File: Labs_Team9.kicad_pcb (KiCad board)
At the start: 2 copper layers, 34.8 x 24.7 mm, 14 parts, among them J1 Conn_02x04_Counter_Clockwise, SW1 SW_Push, SW2 SW_Push, U1 STM32F411RETx, Y1 Crystal_GND24

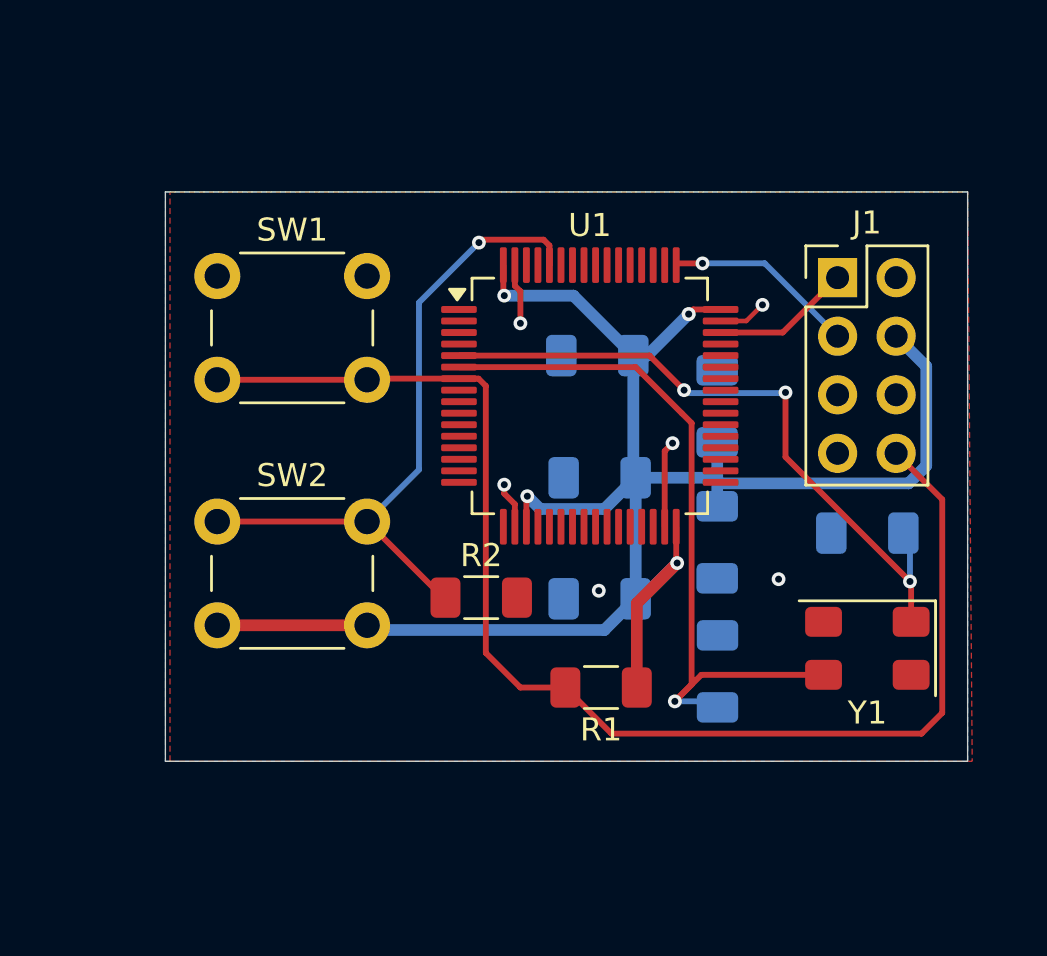
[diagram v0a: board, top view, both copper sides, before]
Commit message: lab2: add schematic and part of the trace
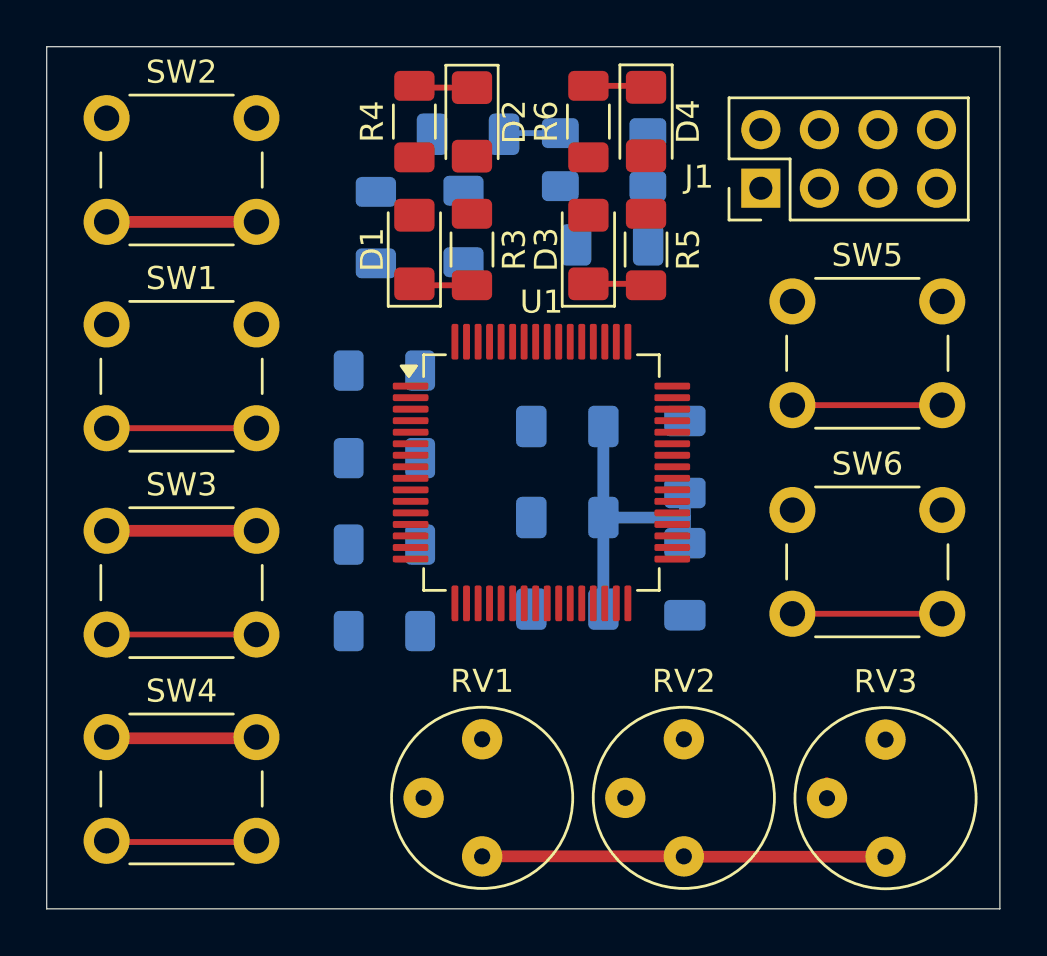
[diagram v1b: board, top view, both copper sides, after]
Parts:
- added D1: LED, LED_SMD:LED_1206_3216Metric_Pad1.42x1.75mm_HandSolder, F.Cu at (148.1, 91.2)
- added D2: LED, LED_SMD:LED_1206_3216Metric_Pad1.42x1.75mm_HandSolder, F.Cu at (150.6, 85.7)
- added D3: LED, LED_SMD:LED_1206_3216Metric_Pad1.42x1.75mm_HandSolder, F.Cu at (155.7, 91.2)
- added D4: LED, LED_SMD:LED_1206_3216Metric_Pad1.42x1.75mm_HandSolder, F.Cu at (158.2, 85.7)
- added R10: 10 kOhm, Resistor_SMD:R_1206_3216Metric_Pad1.30x1.75mm_HandSolder, B.Cu at (150.2, 90.2)
- added R3: 510 Ohm, Resistor_SMD:R_1206_3216Metric_Pad1.30x1.75mm_HandSolder, F.Cu at (150.6, 91.2)
- added R4: 680 Ohm, Resistor_SMD:R_1206_3216Metric_Pad1.30x1.75mm_HandSolder, F.Cu at (148.1, 85.7)
- added R5: 680 Ohm, Resistor_SMD:R_1206_3216Metric_Pad1.30x1.75mm_HandSolder, F.Cu at (158.2, 91.2)
- added R6: 680 Ohm, Resistor_SMD:R_1206_3216Metric_Pad1.30x1.75mm_HandSolder, F.Cu at (155.7, 85.7)
- added R7: 10 kOhm, Resistor_SMD:R_1206_3216Metric_Pad1.30x1.75mm_HandSolder, B.Cu at (146.8, 107.8)
- added R8: 10 kOhm, Resistor_SMD:R_1206_3216Metric_Pad1.30x1.75mm_HandSolder, B.Cu at (146.8, 104.0)
- added R9: 10 kOhm, Resistor_SMD:R_1206_3216Metric_Pad1.30x1.75mm_HandSolder, B.Cu at (146.4, 90.2)
- added RV1: R_Potentiometer, Potentiometer_THT:Potentiometer_Bourns_3339P_Vertical_HandSoldering, F.Cu at (151.0, 117.5)
- added RV2: R_Potentiometer, Potentiometer_THT:Potentiometer_Bourns_3339P_Vertical_HandSoldering, F.Cu at (159.8, 117.5)
- added RV3: R_Potentiometer, Potentiometer_THT:Potentiometer_Bourns_3339P_Vertical_HandSoldering, F.Cu at (168.5, 117.5)
- added SW3: SW_Push, Buttons_Switches_THT:SW_PUSH_6mm, F.Cu at (134.8, 103.4)
- added SW4: SW_Push, Buttons_Switches_THT:SW_PUSH_6mm, F.Cu at (134.8, 112.3)
- added SW5: SW_Push, Buttons_Switches_THT:SW_PUSH_6mm, F.Cu at (164.5, 93.5)
- added SW6: SW_Push, Buttons_Switches_THT:SW_PUSH_6mm, F.Cu at (164.5, 102.5)
- R1, R2, Y1: moved to B.Cu
- moved C6 25.7 mm to (150.4, 86.2), turned to 0 degrees
- moved Y1 24.1 mm to (156.3, 87.3)
- moved SW2 18.1 mm to (134.8, 85.5)
- moved C7 16.7 mm to (156.7, 91.0)
- moved R1 13.7 mm to (146.8, 100.2)
- moved R2 10.7 mm to (146.8, 96.5)
- moved SW1 5.24 mm to (134.8, 94.5)
- moved J1 5.11 mm to (163.1, 88.5), turned to 90 degrees
- moved U1 3.93 mm to (153.6, 100.9)
- moved C3 3.34 mm to (154.7, 98.9)
- moved C5 2.61 mm to (159.8, 100.2)
- moved C2 2.22 mm to (154.7, 102.8)
- moved C4 2.13 mm to (159.8, 105.5)
- moved C1 1.47 mm to (154.7, 106.8)
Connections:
- U1 pad 21: unconnected-(U1-PA5-Pad21) -> Led_Green
- U1 pad 22: unconnected-(U1-PA6-Pad22) -> Led_Orange
- U1 pad 23: unconnected-(U1-PA7-Pad23) -> Led_Red
- U1 pad 24: unconnected-(U1-PC4-Pad24) -> ADC_MCU_1
- U1 pad 25: unconnected-(U1-PC5-Pad25) -> ADC_MCU_2
- U1 pad 26: unconnected-(U1-PB0-Pad26) -> ADC_MCU_3
- U1 pad 39: unconnected-(U1-PC8-Pad39) -> USERB3
- U1 pad 40: unconnected-(U1-PC9-Pad40) -> USERB4
- U1 pad 41: unconnected-(U1-PA8-Pad41) -> Led_Blue
- U1 pad 8: unconnected-(U1-PC0-Pad8) -> USERB1
- U1 pad 9: unconnected-(U1-PC1-Pad9) -> USERB2
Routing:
- net NRST: track 57.1 -> 6.50 mm
- net +3.3V: track 81.1 -> 50.6 mm, vias 4 -> 0
- net OSC_OUT: track 32.4 -> 2.46 mm, vias 1 -> 0
- net BOOT0: track 29.4 -> 0.00 mm, vias 1 -> 0
- net OSC_IN: track 29.3 -> 0.00 mm, vias 3 -> 0
- net GND: track 10.5 -> 0.00 mm, vias 6 -> 0
- net SWCLK: track 8.34 -> 0.00 mm, vias 1 -> 0
- net USERB4: track 0.00 -> 6.50 mm
- net USERB3: track 0.00 -> 6.50 mm
- net USERB2: track 0.00 -> 6.50 mm
- net USERB1: track 0.00 -> 6.50 mm
- net SWDIO: track 6.06 -> 0.00 mm
- net Net-(D2-K): track 0.00 -> 2.53 mm
- net Net-(D4-K): track 0.00 -> 2.53 mm
- net Net-(D3-K): track 0.00 -> 2.53 mm
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- removed copper zone on B.Cu, net GND
- removed copper zone on F.Cu, net GND
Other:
- board size 34.8 x 24.7 mm -> 41.3 x 37.4 mm

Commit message: lab2: add full tracing
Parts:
- moved SW5 9.33 mm to (163.8, 102.8)
- moved SW6 9.03 mm to (163.8, 93.5)
- moved R9 9.02 mm to (155.4, 90.3)
- moved R10 8.77 mm to (159.0, 90.2)
- moved SW2 7.91 mm to (141.2, 90.0), turned to 180 degrees
- moved C7 5.67 mm to (151.1, 90.2)
- moved Y1 5.67 mm to (150.7, 86.5)
- moved C6 4.39 mm to (146.1, 87.0), turned to 90 degrees
- moved R8 3.75 mm to (146.8, 107.8)
- moved R7 3.75 mm to (146.8, 104.0)
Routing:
- net +3.3V: track 50.6 -> 170.0 mm, vias 0 -> 4
- net NRST: track 6.50 -> 47.6 mm, vias 0 -> 2
- net Led_Orange: track 0.00 -> 27.8 mm
- net USERB3: track 6.50 -> 34.0 mm
- net Led_Red: track 0.00 -> 24.1 mm, vias 0 -> 2
- net BOOT0: track 0.00 -> 23.5 mm, vias 0 -> 1
- net USERB2: track 6.50 -> 26.9 mm, vias 0 -> 1
- net SWDIO: track 0.00 -> 19.2 mm
- net OSC_OUT: track 2.46 -> 21.2 mm, vias 0 -> 1
- net Led_Green: track 0.00 -> 18.6 mm, vias 0 -> 2
- net GND: track 0.00 -> 18.3 mm, vias 0 -> 8
- net Led_Blue: track 0.00 -> 17.8 mm, vias 0 -> 2
- net ADC_MCU_3: track 0.79 -> 17.2 mm
- net OSC_IN: track 0.00 -> 14.9 mm, vias 0 -> 1
- net USERB4: track 6.50 -> 20.4 mm
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- added copper zone on B.Cu, net GND
- added copper zone on F.Cu, net GND

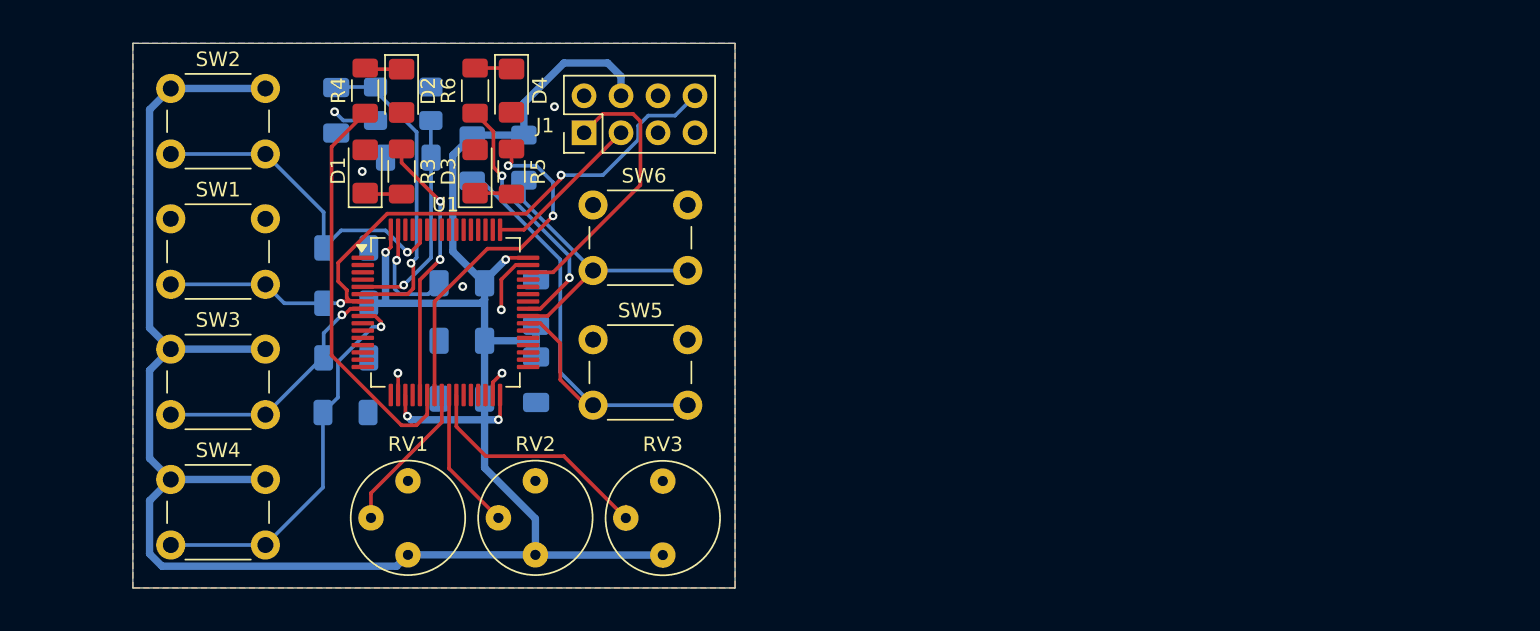
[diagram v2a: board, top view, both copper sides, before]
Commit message: lab3: add schematic
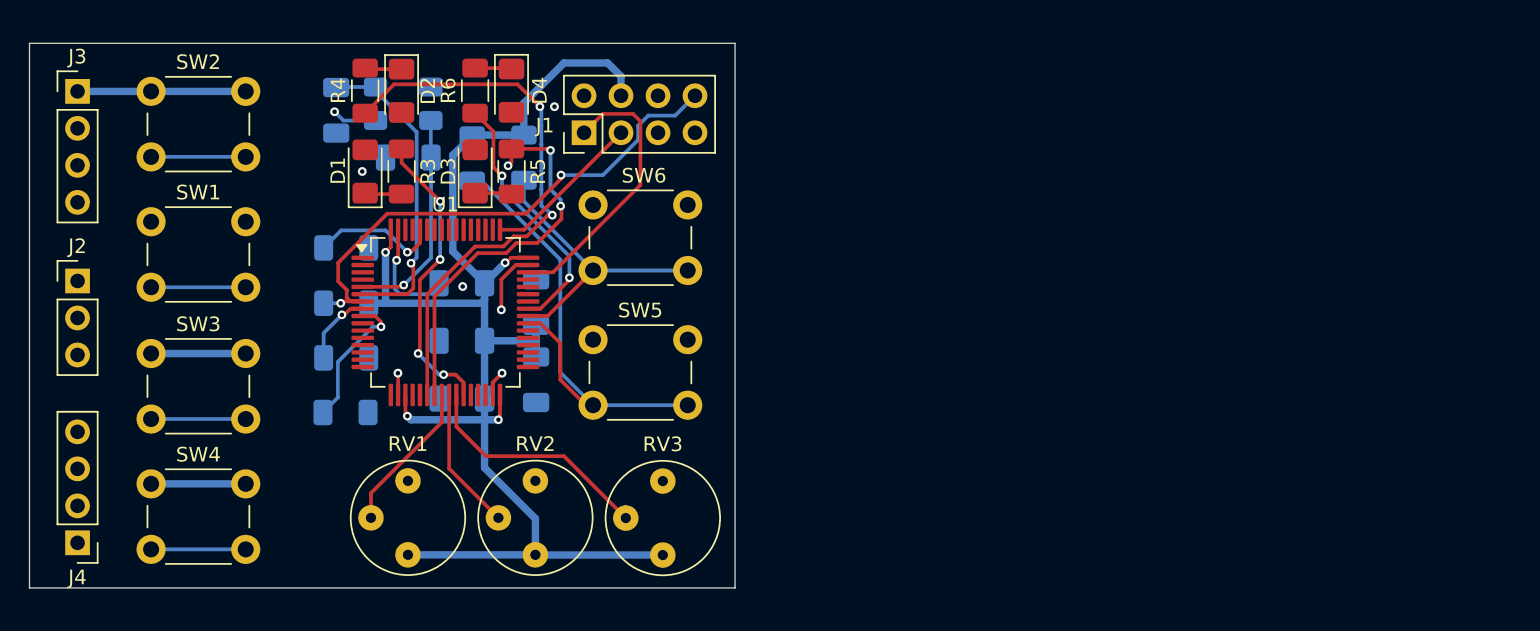
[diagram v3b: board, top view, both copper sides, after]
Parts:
- added J2: Conn_01x03_Pin, Connector_PinHeader_2.54mm:PinHeader_1x03_P2.54mm_Vertical, F.Cu at (128.3, 98.7)
- added J3: Conn_01x04_Pin, Connector_PinHeader_2.54mm:PinHeader_1x04_P2.54mm_Vertical, F.Cu at (128.3, 85.7)
- added J4: Conn_01x04_Pin, Connector_PinHeader_2.54mm:PinHeader_1x04_P2.54mm_Vertical, F.Cu at (128.3, 116.7)
- moved SW4 1.38 mm to (133.4, 112.7)
- moved SW3 1.38 mm to (133.4, 103.7)
- moved SW1 1.36 mm to (133.4, 94.7)
- moved SW2 1.36 mm to (139.9, 90.2)
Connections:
- U1 pad 10: unconnected-(U1-PC2-Pad10) -> SPI_MISO
- U1 pad 11: unconnected-(U1-PC3-Pad11) -> SPI_MOSI
- U1 pad 21: Led_Green -> unconnected-(U1-PA5-Pad21)
- U1 pad 27: unconnected-(U1-PB1-Pad27) -> Led_Green
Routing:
- net +3.3V: track 170.0 -> 121.7 mm
- net Led_Orange: track 27.8 -> 39.1 mm, vias 0 -> 2
- net USERB2: track 26.9 -> 16.1 mm
- net BOOT0: track 23.5 -> 15.4 mm
- net USERB1: track 17.2 -> 11.7 mm
- net NRST: track 47.6 -> 43.1 mm
- net Led_Red: track 24.1 -> 26.7 mm, vias 2 -> 3
- net Led_Green: track 18.6 -> 20.6 mm, vias 2 -> 4
- removed copper zone on B.Cu, net GND
- removed copper zone on F.Cu, net GND
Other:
- board size 41.3 x 37.4 mm -> 48.5 x 37.4 mm

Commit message: lab3: add tracing
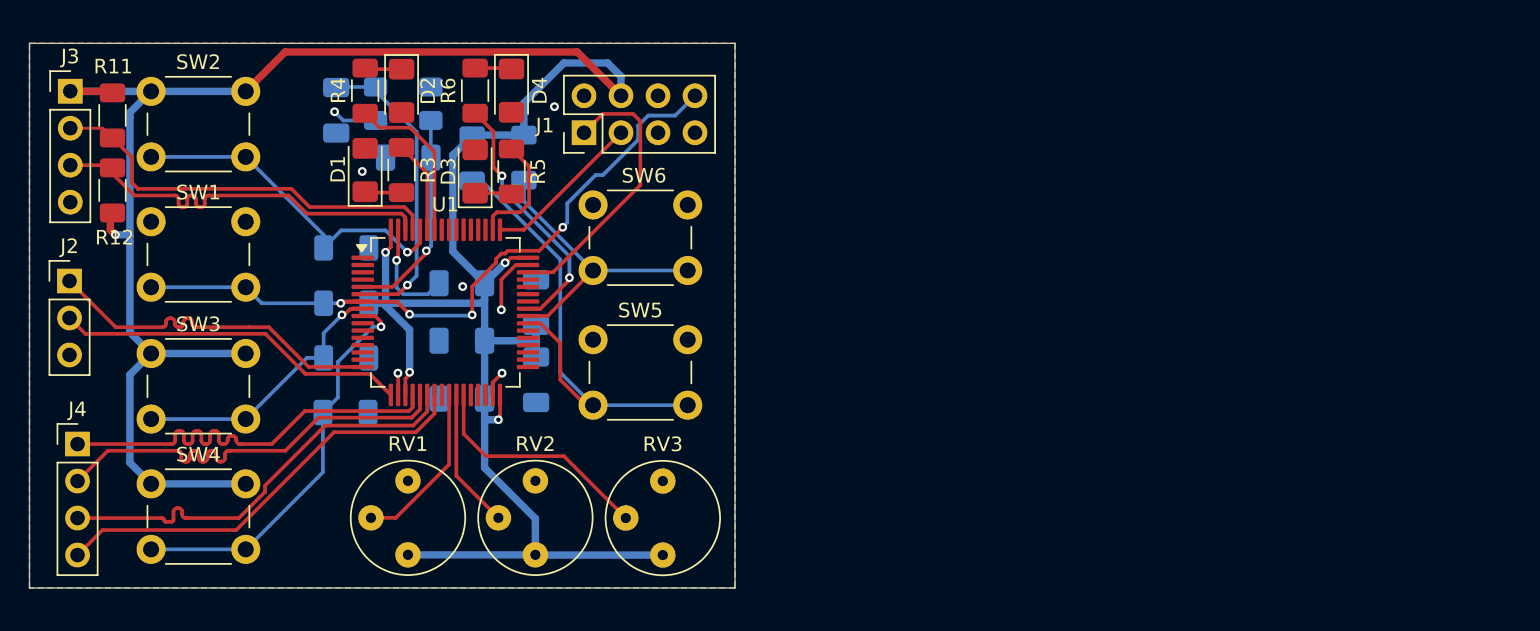
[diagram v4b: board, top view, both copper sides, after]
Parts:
- added R11: 2.2 kOhm, Resistor_SMD:R_1206_3216Metric_Pad1.30x1.75mm_HandSolder, F.Cu at (130.8, 87.3)
- added R12: 2.2 kOhm, Resistor_SMD:R_1206_3216Metric_Pad1.30x1.75mm_HandSolder, F.Cu at (130.8, 92.5)
- moved J4 6.78 mm to (128.3, 109.9), turned to 0 degrees
- moved J2 0.55 mm to (127.8, 98.7)
- moved J3 0.50 mm to (127.8, 85.7)
- moved D1 0.10 mm to (148.1, 91.1)
- moved R3 0.10 mm to (150.6, 91.1)
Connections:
- J2 pad 1: USART_RX -> USART_TX
- J2 pad 2: USART_TX -> USART_RX
- J4 pad 2: SPI_MISO -> SPI_SCK
- J4 pad 3: SPI_MOSI -> SPI_MISO
- J4 pad 4: SPI_SCK -> SPI_MOSI
- U1 pad 10: SPI_MISO -> unconnected-(U1-PC2-Pad10)
- U1 pad 11: SPI_MOSI -> unconnected-(U1-PC3-Pad11)
- U1 pad 16: unconnected-(U1-PA2-Pad16) -> USART_TX
- U1 pad 17: unconnected-(U1-PA3-Pad17) -> USART_RX
- U1 pad 20: unconnected-(U1-PA4-Pad20) -> SPI_NSS
- U1 pad 21: unconnected-(U1-PA5-Pad21) -> SPI_SCK
- U1 pad 22: Led_Orange -> SPI_MISO
- U1 pad 23: Led_Red -> SPI_MOSI
- U1 pad 24: ADC_MCU_1 -> unconnected-(U1-PC4-Pad24)
- U1 pad 25: ADC_MCU_2 -> ADC_MCU_1
- U1 pad 26: ADC_MCU_3 -> ADC_MCU_2
- U1 pad 27: Led_Green -> ADC_MCU_3
- U1 pad 50: unconnected-(U1-PA15-Pad50) -> Led_Red
- U1 pad 58: unconnected-(U1-PB6-Pad58) -> Led_Orange
- U1 pad 59: unconnected-(U1-PB7-Pad59) -> Led_Green
- U1 pad 61: unconnected-(U1-PB8-Pad61) -> I2C_SCL
- U1 pad 62: unconnected-(U1-PB9-Pad62) -> I2C_SDA
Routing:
- net +3.3V: track 121.7 -> 184.8 mm, vias 4 -> 5
- net SPI_MOSI: track 0.00 -> 29.8 mm
- net SPI_MISO: track 0.00 -> 29.8 mm
- net SPI_SCK: track 0.00 -> 29.7 mm
- net SPI_NSS: track 0.00 -> 29.6 mm
- net I2C_SDA: track 0.00 -> 28.0 mm
- net I2C_SCL: track 0.00 -> 28.0 mm
- net Led_Orange: track 39.1 -> 11.2 mm, vias 2 -> 0
- net USART_RX: track 0.00 -> 24.3 mm
- net USART_TX: track 0.00 -> 24.1 mm
- net Led_Red: track 26.7 -> 8.02 mm, vias 3 -> 0
- net Led_Green: track 20.6 -> 6.38 mm, vias 4 -> 0
- net USERB2: track 16.1 -> 27.7 mm
- net BOOT0: track 15.4 -> 23.9 mm
- net USERB1: track 11.7 -> 18.7 mm
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- added copper zone on B.Cu, net GND
- added copper zone on F.Cu, net GND

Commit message: lab4: add schematic and tracing
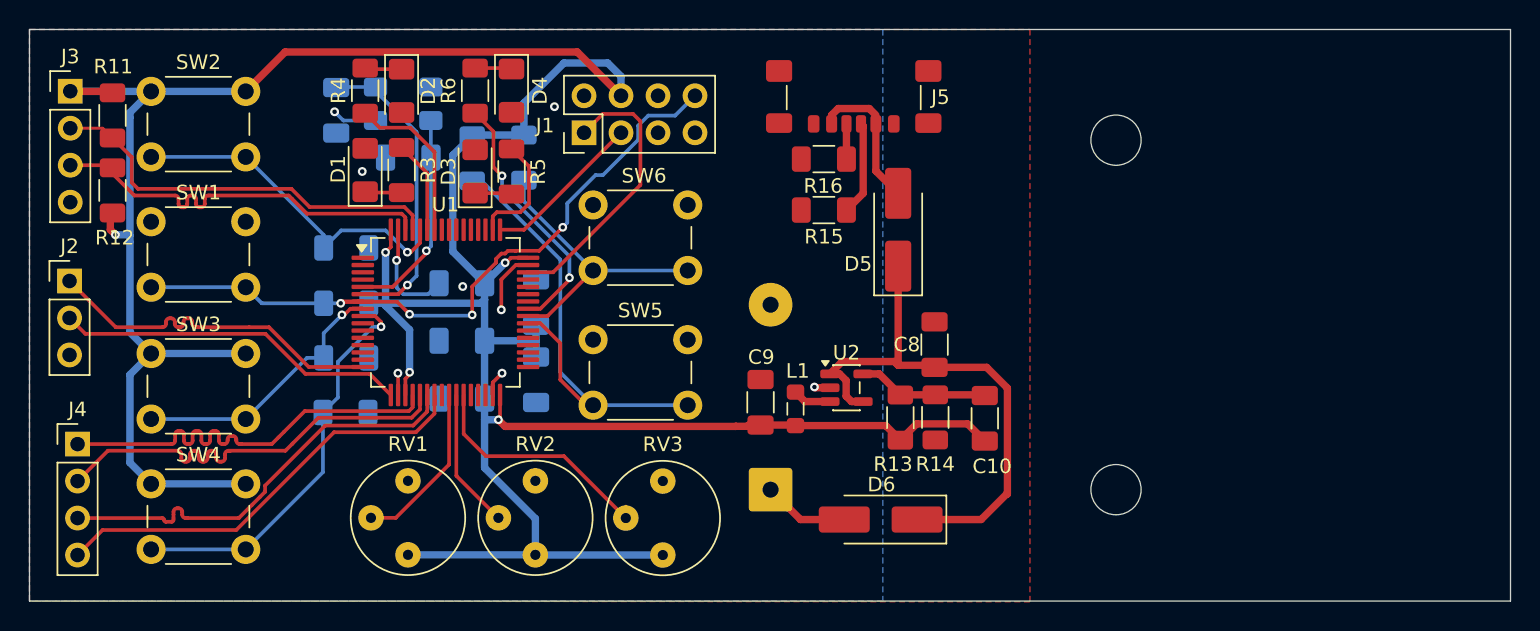
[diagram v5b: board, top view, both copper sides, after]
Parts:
- added BT1: Battery, Battery:BatteryHolder_Keystone_2479_3xAAA, B.Cu at (175.9, 113.0)
- added C10: DNM, Capacitor_SMD:C_1206_3216Metric_Pad1.33x1.80mm_HandSolder, F.Cu at (190.7, 108.2)
- added C8: 10 μF, Capacitor_SMD:C_1206_3216Metric_Pad1.33x1.80mm_HandSolder, F.Cu at (187.2, 103.1)
- added C9: 10 μF, Capacitor_SMD:C_1206_3216Metric_Pad1.33x1.80mm_HandSolder, F.Cu at (175.2, 107.0)
- added D5: SS34, Diode_SMD:D_SMA_Handsoldering, F.Cu at (184.7, 95.2)
- added D6: SS34, Diode_SMD:D_SMA_Handsoldering, F.Cu at (183.5, 115.1)
- added J5: USB_C_Receptacle_PowerOnly_6P, Connector_USB:USB_C_Receptacle_GCT_USB4135-GF-A_6P_TopMnt_Horizontal, F.Cu at (181.7, 84.9)
- added L1: 2.2 μH, Inductor_SMD:L_0805_2012Metric_Pad1.05x1.20mm_HandSolder, F.Cu at (177.7, 107.5)
- added R13: 91 kOhm, Resistor_SMD:R_1206_3216Metric_Pad1.30x1.75mm_HandSolder, F.Cu at (184.8, 108.1)
- added R14: 20 kOhm, Resistor_SMD:R_1206_3216Metric_Pad1.30x1.75mm_HandSolder, F.Cu at (187.2, 108.1)
- added R15: 5.1 kOhm, Resistor_SMD:R_1206_3216Metric_Pad1.30x1.75mm_HandSolder, F.Cu at (179.6, 93.8)
- added R16: 5.1 kOhm, Resistor_SMD:R_1206_3216Metric_Pad1.30x1.75mm_HandSolder, F.Cu at (179.6, 90.3)
- added U2: TLV62569DBV, Package_TO_SOT_SMD:SOT-23-5, F.Cu at (181.2, 106.0)
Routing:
- net Net-(D5-K): track 0.00 -> 38.0 mm
- net +3.3V: track 184.8 -> 219.8 mm
- net Net-(D5-A): track 0.00 -> 9.42 mm
- net Net-(U2-FB): track 0.00 -> 8.99 mm
- net Net-(J5-CC1): track 0.00 -> 6.46 mm
- net Net-(BT1-+): track 0.00 -> 5.91 mm
- net Net-(U2-SW): track 0.00 -> 2.63 mm
- net Net-(J5-CC2): track 0.00 -> 2.42 mm
- net GND: track 18.1 -> 19.2 mm, vias 8 -> 9
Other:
- board size 48.5 x 37.4 mm -> 101.7 x 39.2 mm
